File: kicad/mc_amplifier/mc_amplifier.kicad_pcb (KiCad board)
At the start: 2 copper layers, 35 x 13 mm, 13 parts

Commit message: Добавил новую версию усилителя mc_amplifier_rev_1.
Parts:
- added C5: 47 мк 25 В, IWsmd_case:CASE_D, F.Cu at (196.8, 123.2)
- added R10: 0, IWsmd_case:SMD0805, B.Cu at (196.6, 119.1)
- added R6: 50 к, IWsmd_case:BOURNS_3224J, B.Cu at (189.2, 122.9)
- added R7: 10 к 1%, IWsmd_case:SMD0805, B.Cu at (193.3, 122.4)
- added R8: 10 к 1%, IWsmd_case:SMD0805, B.Cu at (196.6, 123.2)
- added R9: 10 к 1%, IWsmd_case:SMD0805, B.Cu at (199.9, 124.2)
- C1, R1, R4: footprint SMD0805 -> IWsmd_case:SMD0805
- C4: value 47 мк -> 47 мк 25 В; footprint CASE_C -> IWsmd_case:CASE_D; moved to F.Cu
- DA1: value LME49720MA -> NE5532AD
- R2: footprint SMD0805 -> IWsmd_case:SMD0805; moved to B.Cu
- R3: value 100 к -> 51 к 1%; footprint SMD0805 -> IWsmd_case:SMD0805
- R5: value 5.1 к -> 5.1 к 1%; footprint SMD0805 -> IWsmd_case:SMD0805; moved to B.Cu
- moved R4 13.9 mm to (180.3, 126.2)
- moved R5 11.6 mm to (184.5, 118.4), turned to 0 degrees
- moved C4 9.14 mm to (190.5, 123.4)
- moved C3 5.83 mm to (183.5, 120.8)
- moved R2 5.14 mm to (180.3, 122.2)
- moved R3 4.96 mm to (188.5, 126.1), turned to 0 degrees
- moved DA1 4.89 mm to (184.4, 124.0)
- moved R1 3.64 mm to (180.3, 122.2), turned to 90 degrees
- moved C1 2.29 mm to (180.3, 126.2)
- moved VD1 2.05 mm to (177.5, 127.0)
- moved C2 2.03 mm to (181.6, 118.4)
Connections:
- net /+10V renamed /+9V
- C3 pad 1: N-000004 -> Net-(C3-Pad1)
- DA1 pad 7: N-000004 -> Net-(C3-Pad1)
- R3 pad 2: N-000004 -> Net-(R3-Pad2)
- XP2 pad 2: N-000004 -> Net-(R10-Pad2)
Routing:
- net Net-(C3-Pad1): track 0.00 -> 31.3 mm, vias 0 -> 3
- net N-000004: track 20.6 -> 0.00 mm, vias 1 -> 0
- net Net-(DA1-Pad2): track 24.3 -> 14.2 mm, vias 1 -> 0
- net Net-(R10-Pad2): track 0.00 -> 9.59 mm
- net Net-(C1-Pad1): track 17.0 -> 8.52 mm
- net /GND: track 5.58 -> 12.8 mm
- net Net-(C5-Pad2): track 0.00 -> 4.79 mm, vias 0 -> 1
- net Net-(R3-Pad2): track 0.00 -> 3.60 mm
- net Net-(R7-Pad2): track 0.00 -> 2.36 mm
- net Net-(R1-Pad1): track 9.48 -> 7.15 mm
- net Net-(C3-Pad2): track 13.8 -> 11.7 mm
- net /+9V: track 24.9 -> 26.7 mm
- net Net-(C4-Pad1): track 5.58 -> 6.72 mm
- net Net-(DA1-Pad1): track 11.9 -> 11.2 mm

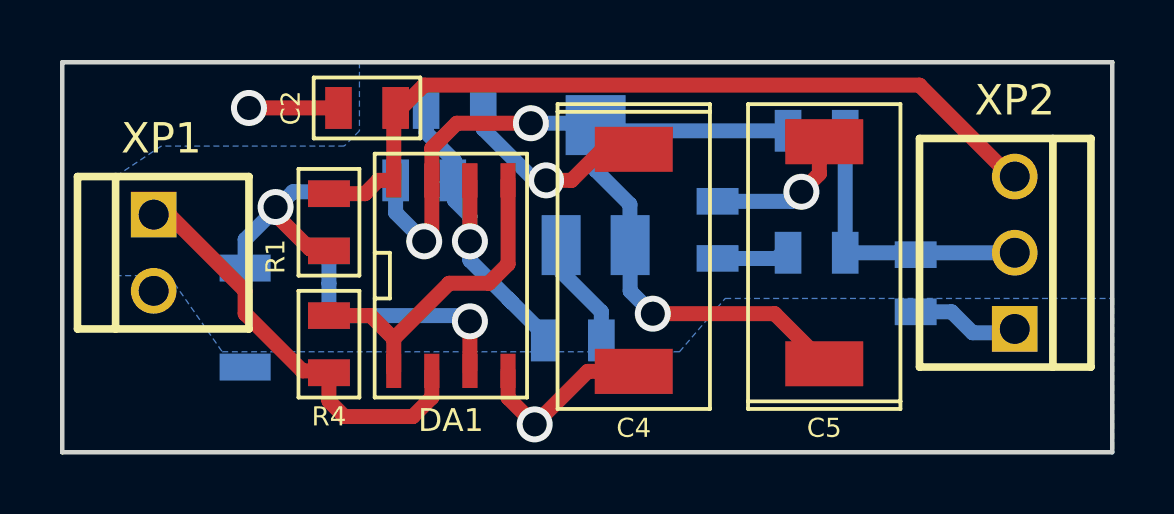
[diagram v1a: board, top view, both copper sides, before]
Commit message: Порпвил схему и отравил плату mc_amplifier rev1 на изготовление.
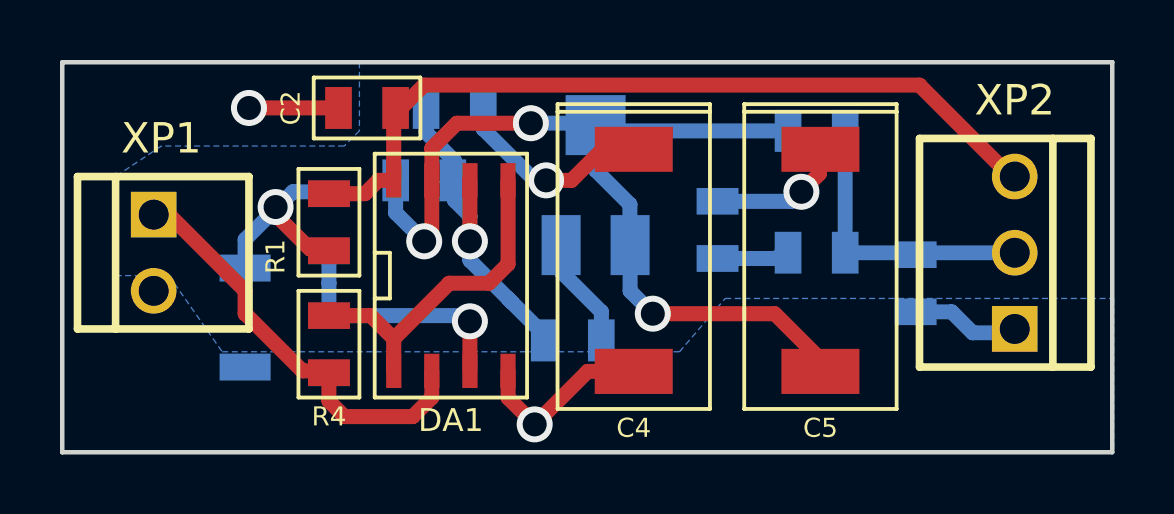
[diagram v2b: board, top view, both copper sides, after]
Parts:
- R7, R8, R9: value 10 к 1% -> 1 к 1%
- moved C5 0.28 mm to (196.7, 123.4), turned to 270 degrees
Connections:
- C5 pad 1: Net-(C3-Pad1) -> Net-(C5-Pad1)
- C5 pad 2: Net-(C5-Pad2) -> Net-(C3-Pad1)
- R7 pad 1: Net-(C5-Pad2) -> Net-(C5-Pad1)
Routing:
- net Net-(C5-Pad2): track 4.79 -> 0.00 mm, vias 1 -> 0
- net Net-(C5-Pad1): track 0.00 -> 4.79 mm, vias 0 -> 1

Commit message: Поправил схему и отравил плату mc_amplifier rev1 на изготовление.
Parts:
- R3: value 51 к 1% -> 5.1 к 1%
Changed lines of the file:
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@@
       (effects (font (size 0.635 0.635) (thickness 0.127)) (justify mirror))
     )
-    (fp_text value "51 к 1%" (at 0.254 -1.524) (layer B.SilkS) hide
+    (fp_text value "5.1 к 1%" (at 0.254 -1.524) (layer B.SilkS) hide
       (effects (font (size 0.635 0.635) (thickness 0.127)) (justify mirror))
     )
@@
   (segment (start 185.4835 118.364) (end 185.4835 119.0625) (width 0.5) (layer B.Cu) (net 6))
   (segment (start 185.4835 119.0625) (end 187.198 120.777) (width 0.5) (layer B.Cu) (net 6))
-  (segment (start 193.294 121.4755) (end 195.7705 121.4755) (width 0.5) (layer B.Cu) (net 13))
-  (via (at 196.088 121.158) (size 1.2) (drill 0.8) (layers F.Cu B.Cu) (net 13))
-  (segment (start 195.7705 121.4755) (end 196.088 121.158) (width 0.5) (layer B.Cu) (net 13))
-  (segment (start 196.687999 120.558001) (end 196.687999 119.542001) (width 0.5) (layer F.Cu) (net 13))
-  (segment (start 196.088 121.158) (end 196.687999 120.558001) (width 0.5) (layer F.Cu) (net 13))
   (segment (start 182.499 126.0555) (end 184.3485 124.206) (width 0.5) (layer F.Cu) (net 7))
   (segment (start 182.499 127.127) (end 182.499 126.0555) (width 0.5) (layer F.Cu) (net 7))
@@
   (segment (start 199.898 123.19) (end 197.612 123.19) (width 0.5) (layer B.Cu) (net 12))
   (segment (start 197.5485 123.19) (end 197.5485 119.1895) (width 0.5) (layer B.Cu) (net 12))
+  (segment (start 193.294 121.4755) (end 195.7705 121.4755) (width 0.5) (layer B.Cu) (net 13))
+  (via (at 196.088 121.158) (size 1.2) (drill 0.8) (layers F.Cu B.Cu) (net 13))
+  (segment (start 195.7705 121.4755) (end 196.088 121.158) (width 0.5) (layer B.Cu) (net 13))
+  (segment (start 196.687999 120.558001) (end 196.687999 119.542001) (width 0.5) (layer F.Cu) (net 13))
+  (segment (start 196.088 121.158) (end 196.687999 120.558001) (width 0.5) (layer F.Cu) (net 13))
   (zone (net 1) (net_name /GND) (layer B.Cu) (hatch edge 0.508)
     (connect_pads (clearance 0.254))
